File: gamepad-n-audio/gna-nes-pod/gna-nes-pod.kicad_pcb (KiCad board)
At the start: 2 copper layers, 78 x 43 mm, 12 parts, among them J1 NES, J2 NES, J3 Gamepads, J4 NES, J5 NES

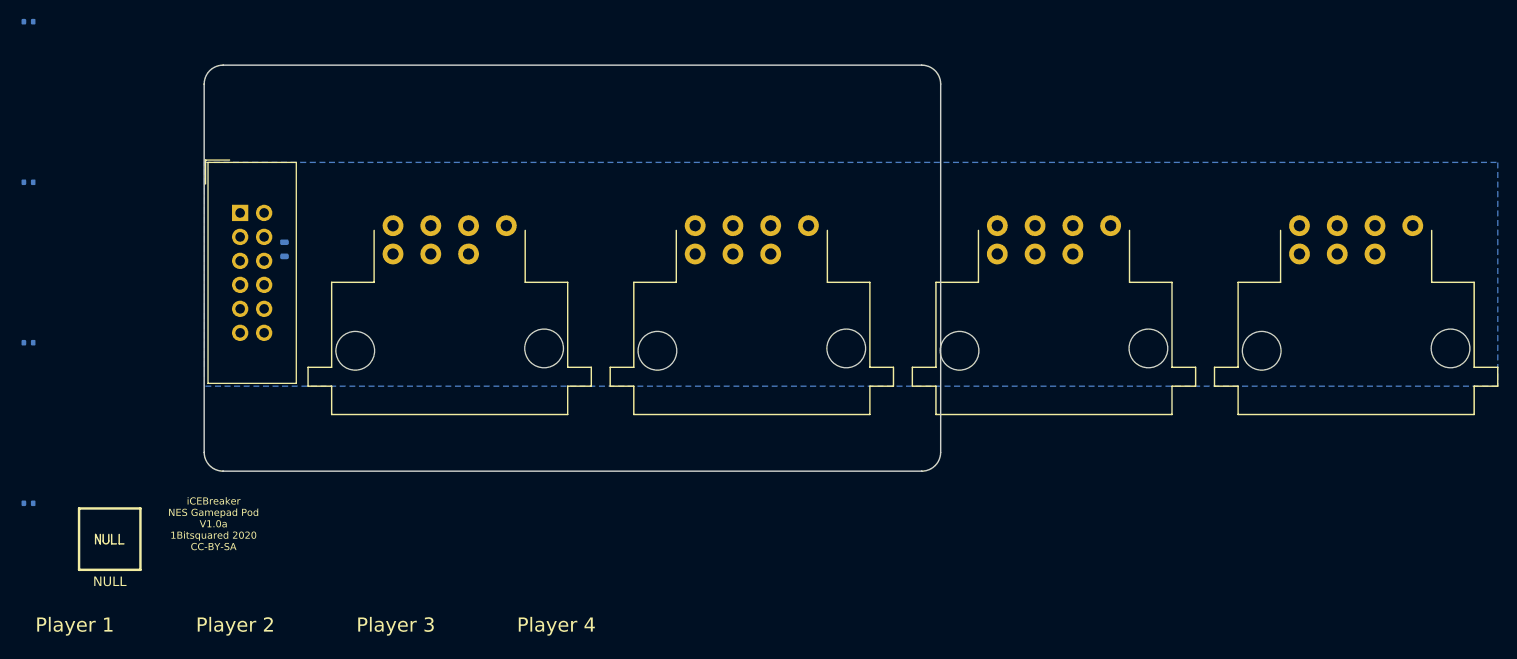
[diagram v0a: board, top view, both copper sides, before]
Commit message: gna NES pod: Finished layout.
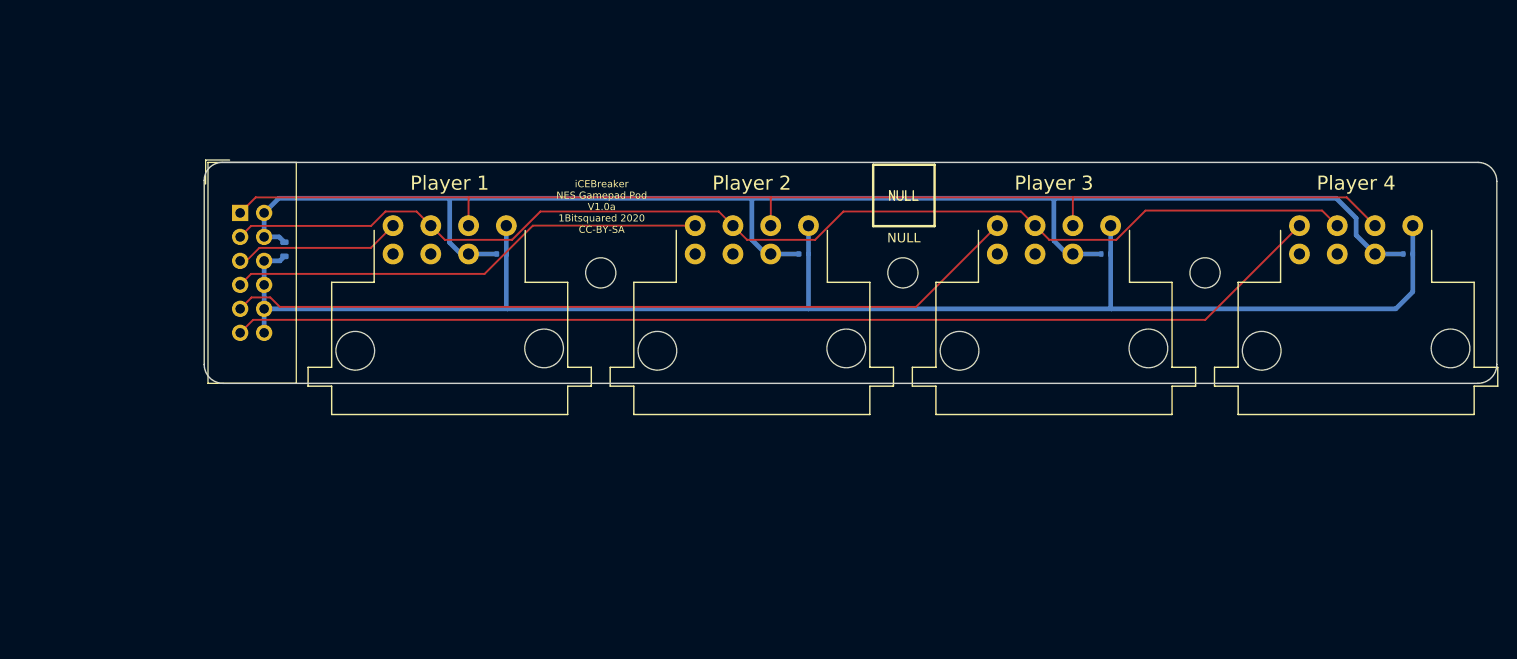
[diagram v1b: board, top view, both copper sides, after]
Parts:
- added REF**: MountingHole_3.2mm_M3, MountingHole:MountingHole_3.2mm_M3, F.Cu at (143.4, 74.0)
- added REF**: MountingHole_3.2mm_M3, MountingHole:MountingHole_3.2mm_M3, F.Cu at (111.4, 74.0)
- added REF**: MountingHole_3.2mm_M3, MountingHole:MountingHole_3.2mm_M3, F.Cu at (79.4, 74.0)
- moved C5 148.5 mm to (164.9, 72.0)
- moved C4 114.5 mm to (132.9, 72.0)
- moved REF** 92.4 mm to (111.5, 65.8), turned to 180 degrees
- moved REF** 91.6 mm to (111.5, 65.8)
- moved C3 82.5 mm to (100.9, 72.0)
- moved C2 55.8 mm to (68.9, 72.0)
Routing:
- net GND: track 0.00 -> 165.9 mm
- net VCC: track 0.00 -> 160.1 mm
- net /CLK: track 0.00 -> 131.1 mm
- net /LATCH: track 0.00 -> 125.5 mm
- net /GPD3: track 0.00 -> 116.9 mm
- net /GPD2: track 0.00 -> 84.7 mm
- net /GPD1: track 0.00 -> 50.8 mm
- net /GPD0: track 0.00 -> 17.7 mm
- removed copper zone on B.Cu, net GND
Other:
- board size 78 x 43 mm -> 136.9 x 23.4 mm
